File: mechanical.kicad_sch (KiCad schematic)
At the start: 0 parts

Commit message: SCH[Cleaning]:Updated Connectors not sure still, added sprate bat and ground connections, updated commincation conncetors. PCB[Layout]:Inital layout of compents need to fit on board size once tap connecton method is decided.
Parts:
- added FID1, FID2, FID3: Fiducial, Fiducial:Fiducial_0.5mm_Mask1mm, symbol Mechanical:Fiducial
- added H1, H2, H3, H4: MountingHole, MountingHole:MountingHole_3.2mm_M3, symbol Mechanical:MountingHole
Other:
- note added: "Fiducials"
- note added: "Mounting Holes"

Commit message: PCB[DRC, Grouding]: Need to seprate top ground planes, and possibliy bring caps to top side, started adressing drc errors. To fix: Via sizing on bms chip, ground planes and senstive grounds, trace matching sens and bal, connector finilzation, temp routing, logos and other silk screen, test points, review!
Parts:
- added H5: MountingHole, MountingHole:MountingHole_3.2mm_M3, symbol Mechanical:MountingHole
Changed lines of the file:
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@@
 	(rectangle
 		(start 101.6 83.82)
-		(end 139.7 101.6)
+		(end 139.7 109.22)
 		(stroke
 			(width 0.254)
@@
 					(unit 1)
 				)
+			)
+		)
+	)
+	(symbol
+		(lib_id "Mechanical:MountingHole")
+		(at 106.68 104.14 0)
+		(unit 1)
+		(body_style 1)
+		(exclude_from_sim no)
+		(in_bom no)
+		(on_board yes)
+		(in_pos_files yes)
+		(dnp no)
+		(fields_autoplaced yes)
+		(property "Reference" "H5"
+			(at 109.22 102.87 0)
+			(show_name no)
+			(do_not_autoplace no)
+			(effects
+				(font
+					(size 1.27 1.27)
+				)
+				(justify left)
+			)
+		)
+		(property "Value" "MountingHole"
+			(at 109.22 105.41 0)
+			(show_name no)
+			(do_not_autoplace no)
+			(effects
+				(font
+					(size 1.27 1.27)
+				)
+				(justify left)
+			)
+		)
+		(property "Footprint" "MountingHole:MountingHole_3.2mm_M3"
+			(at 106.68 104.14 0)
+			(hide yes)
+			(show_name no)
+			(do_not_autoplace no)
+			(effects
+				(font
+					(size 1.27 1.27)
+				)
+			)
+		)
+		(property "Datasheet" ""
+			(at 106.68 104.14 0)
+			(hide yes)
+			(show_name no)
+			(do_not_autoplace no)
+			(effects
+				(font
+					(size 1.27 1.27)
+				)
+			)
+		)
+		(property "Description" "Mounting Hole without connection"
+			(at 106.68 104.14 0)
+			(hide yes)
+			(show_name no)
+			(do_not_autoplace no)
+			(effects
+				(font
+					(size 1.27 1.27)
+				)
+			)
+		)
+		(instances
+			(project "bms_slave"
+				(path "/f9e05184-c88b-4a88-ae9c-ab2bdb32be7c/c5103ceb-5325-4a84-a025-9638a412984e/f4a7f626-808e-4d0f-b4d4-b24a2b39d327"
+					(reference "H5")
+					(unit 1)
+				)

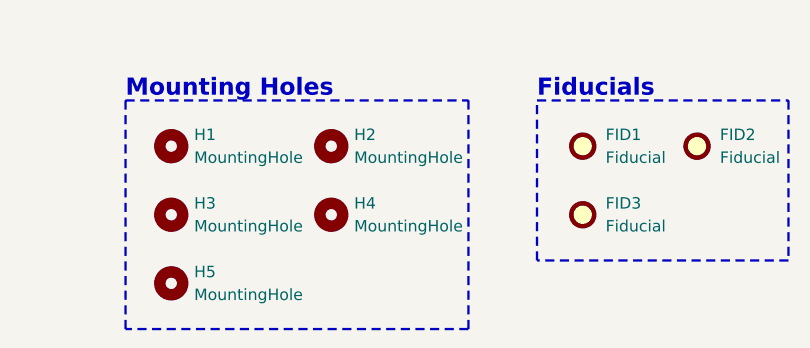
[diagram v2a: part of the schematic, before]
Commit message: PCB[Holes]: Updated hole positioning.
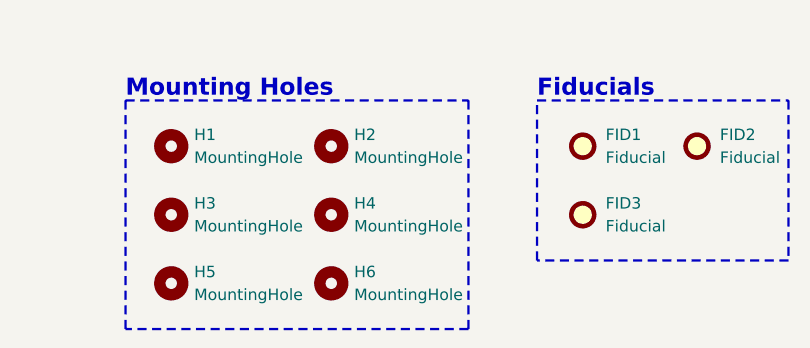
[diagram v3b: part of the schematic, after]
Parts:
- added H6: MountingHole, MountingHole:MountingHole_3.2mm_M3, symbol Mechanical:MountingHole
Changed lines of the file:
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@@
+	)
+	(symbol
+		(lib_id "Mechanical:MountingHole")
+		(at 124.46 104.14 0)
+		(unit 1)
+		(body_style 1)
+		(exclude_from_sim no)
+		(in_bom no)
+		(on_board yes)
+		(in_pos_files yes)
+		(dnp no)
+		(fields_autoplaced yes)
+		(property "Reference" "H6"
+			(at 127 102.87 0)
+			(show_name no)
+			(do_not_autoplace no)
+			(effects
+				(font
+					(size 1.27 1.27)
+				)
+				(justify left)
+			)
+		)
+		(property "Value" "MountingHole"
+			(at 127 105.41 0)
+			(show_name no)
+			(do_not_autoplace no)
+			(effects
+				(font
+					(size 1.27 1.27)
+				)
+				(justify left)
+			)
+		)
+		(property "Footprint" "MountingHole:MountingHole_3.2mm_M3"
+			(at 124.46 104.14 0)
+			(hide yes)
+			(show_name no)
+			(do_not_autoplace no)
+			(effects
+				(font
+					(size 1.27 1.27)
+				)
+			)
+		)
+		(property "Datasheet" ""
+			(at 124.46 104.14 0)
+			(hide yes)
+			(show_name no)
+			(do_not_autoplace no)
+			(effects
+				(font
+					(size 1.27 1.27)
+				)
+			)
+		)
+		(property "Description" "Mounting Hole without connection"
+			(at 124.46 104.14 0)
+			(hide yes)
+			(show_name no)
+			(do_not_autoplace no)
+			(effects
+				(font
+					(size 1.27 1.27)
+				)
+			)
+		)
+		(instances
+			(project "bms_slave"
+				(path "/f9e05184-c88b-4a88-ae9c-ab2bdb32be7c/c5103ceb-5325-4a84-a025-9638a412984e/f4a7f626-808e-4d0f-b4d4-b24a2b39d327"
+					(reference "H6")
+					(unit 1)
+				)
+			)
+		)
 	)
 	(symbol

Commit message: PCB[Silkscreen, DRC]: Though all drc erros minus one, not an issue just need to clear. Added silk logos
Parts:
- added G1: SAE Electric logo, remote_sae_electric_logo:SAE_Electric_Logo_10mm, symbol remote_sae_electric_logo:LOGO
- added G2: BMD Logo, remote_bmd_logo:BDM_Logo_50mm, symbol remote_bmd_logo:BMD LOGO
- added G3: Sparky Logo, remote_sparky_logo:Sparky_Logo_50mm, symbol remote_sparky_logo:LOGO

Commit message: PCB[Grounding, Heat]: Added some more pours for heat considerations for bjt, stiched more vias for heat consideration on balanace resistors. SCH[Notes, Block Diagram]: Working on spelling and notes updates, started block diagram.
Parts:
- removed G3: Sparky Logo, remote_sparky_logo:Sparky_Logo_50mm, symbol remote_sparky_logo:LOGO
- renumbered FID3 to FID2, FID2 to FID3, H3 to H2, H5 to H3, H2 to H4, H4 to H5
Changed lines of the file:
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@@
 		(dnp no)
 		(fields_autoplaced yes)
-		(property "Reference" "FID2"
+		(property "Reference" "FID3"
 			(at 167.64 87.63 0)
 			(show_name no)
@@
 			(project "bms_slave"
 				(path "/f9e05184-c88b-4a88-ae9c-ab2bdb32be7c/c5103ceb-5325-4a84-a025-9638a412984e/f4a7f626-808e-4d0f-b4d4-b24a2b39d327"
-					(reference "FID2")
+					(reference "FID3")
 					(unit 1)
 				)
@@
 		(dnp no)
 		(fields_autoplaced yes)
-		(property "Reference" "H5"
+		(property "Reference" "H3"
 			(at 109.22 102.87 0)
 			(show_name no)
@@
 			(project "bms_slave"
 				(path "/f9e05184-c88b-4a88-ae9c-ab2bdb32be7c/c5103ceb-5325-4a84-a025-9638a412984e/f4a7f626-808e-4d0f-b4d4-b24a2b39d327"
-					(reference "H5")
+					(reference "H3")
 					(unit 1)
 				)
@@
 		(dnp no)
 		(fields_autoplaced yes)
-		(property "Reference" "H3"
+		(property "Reference" "H2"
 			(at 109.22 95.25 0)
 			(show_name no)
@@
 			(project "bms_slave"
 				(path "/f9e05184-c88b-4a88-ae9c-ab2bdb32be7c/c5103ceb-5325-4a84-a025-9638a412984e/f4a7f626-808e-4d0f-b4d4-b24a2b39d327"
-					(reference "H3")
+					(reference "H2")
 					(unit 1)
 				)
@@
 		(dnp no)
 		(fields_autoplaced yes)
-		(property "Reference" "H4"
+		(property "Reference" "H5"
 			(at 127 95.25 0)
 			(show_name no)
@@
 			(project "bms_slave"
 				(path "/f9e05184-c88b-4a88-ae9c-ab2bdb32be7c/c5103ceb-5325-4a84-a025-9638a412984e/f4a7f626-808e-4d0f-b4d4-b24a2b39d327"
-					(reference "H4")
+					(reference "H5")
 					(unit 1)
 				)
@@
 		(dnp no)
 		(fields_autoplaced yes)
-		(property "Reference" "H2"
+		(property "Reference" "H4"
 			(at 127 87.63 0)
 			(show_name no)
@@
 			(project "bms_slave"
 				(path "/f9e05184-c88b-4a88-ae9c-ab2bdb32be7c/c5103ceb-5325-4a84-a025-9638a412984e/f4a7f626-808e-4d0f-b4d4-b24a2b39d327"
-					(reference "H2")
+					(reference "H4")
 					(unit 1)
 				)
@@
 		(dnp no)
 		(fields_autoplaced yes)
-		(property "Reference" "FID3"
+		(property "Reference" "FID2"
 			(at 154.94 95.25 0)
 			(show_name no)
@@
 			(project "bms_slave"
 				(path "/f9e05184-c88b-4a88-ae9c-ab2bdb32be7c/c5103ceb-5325-4a84-a025-9638a412984e/f4a7f626-808e-4d0f-b4d4-b24a2b39d327"
-					(reference "FID3")
+					(reference "FID2")
 					(unit 1)
 				)
-			)
-		)
-	)
-	(symbol
-		(lib_id "remote_sparky_logo:LOGO")
-		(at 214.63 129.54 0)
-		(unit 1)
-		(body_style 0)
-		(exclude_from_sim no)
-		(in_bom yes)
-		(on_board yes)
-		(in_pos_files yes)
-		(dnp no)
-		(property "Reference" "G3"
-			(at 214.63 105.1737 0)
-			(hide yes)
-			(show_name no)
-			(do_not_autoplace no)
-			(effects
-				(font
-					(size 1.27 1.27)
-				)
-			)
-		)
-		(property "Value" "Sparky Logo"
-			(at 209.55 106.68 0)
-			(show_name no)
-			(do_not_autoplace no)
-			(effects
-				(font
-					(size 1.27 1.27)
-				)
-				(justify left)
-			)
-		)
-		(property "Footprint" "remote_sparky_logo:Sparky_Logo_50mm"
-			(at 214.63 129.54 0)
-			(hide yes)
-			(show_name no)
-			(do_not_autoplace no)
-			(effects
-				(font
-					(size 1.27 1.27)
-				)
-			)
-		)
-		(property "Datasheet" "N/A"
-			(at 214.63 129.54 0)
-			(hide yes)
-			(show_name no)
-			(do_not_autoplace no)
-			(effects
-				(font
-					(size 1.27 1.27)
-				)
-			)
-		)
-		(property "Description" "Sparky Logo."
-			(at 214.63 129.54 0)
-			(hide yes)
-			(show_name no)
-			(do_not_autoplace no)
-			(effects
-				(font
-					(size 1.27 1.27)
-				)
-			)
-		)
-		(property "Manufacturer" "BDM"
-			(at 214.63 129.54 0)
-			(hide yes)
-			(show_name no)
-			(do_not_autoplace no)
-			(effects
-				(font
-					(size 1.27 1.27)
-				)
-			)
-		)
-		(property "Manufacturer Part Number" "Sparky Logo"
-			(at 214.63 129.54 0)
-			(hide yes)
-			(show_name no)
-			(do_not_autoplace no)
-			(effects
-				(font
-					(size 1.27 1.27)
-				)
-			)
-		)
-		(property "Vendor" ""
-			(at 214.63 129.54 0)
-			(hide yes)
-			(show_name no)
-			(do_not_autoplace no)
-			(effects
-				(font
-					(size 1.27 1.27)
-				)
-			)
-		)
-		(property "Vendor Part Number" ""
-			(at 214.63 129.54 0)
-			(hide yes)
-			(show_name no)
-			(do_not_autoplace no)
-			(effects
-				(font
-					(size 1.27 1.27)
-				)
-			)
-		)
-		(property "Mass (g)" ""
-			(at 214.63 129.54 0)
-			(hide yes)
-			(show_name no)
-			(do_not_autoplace no)
-			(effects
-				(font
-					(size 1.27 1.27)
-				)
-			)
-		)
-		(property "RQjC (C/W)" ""
-			(at 214.63 129.54 0)
-			(hide yes)
-			(show_name no)
-			(do_not_autoplace no)
-			(effects
-				(font
-					(size 1.27 1.27)
-				)
-			)
-		)
-		(property "RQjC_top (C/W)" ""
-			(at 214.63 129.54 0)
-			(hide yes)
-			(show_name no)
-			(do_not_autoplace no)
-			(effects
-				(font
-					(size 1.27 1.27)
-				)
-			)
-		)
-		(property "Temp_max (C)" ""
-			(at 214.63 129.54 0)
-			(hide yes)
-			(show_name no)
-			(do_not_autoplace no)
-			(effects
-				(font
-					(size 1.27 1.27)
-				)
-			)
-		)
-		(property "Temp_min (C)" ""
-			(at 214.63 129.54 0)
-			(hide yes)
-			(show_name no)
-			(do_not_autoplace no)
-			(effects
-				(font
-					(size 1.27 1.27)
-				)
-			)
-		)
-		(property "Power Dissipation (W)" ""
-			(at 214.63 129.54 0)
-			(hide yes)
-			(show_name no)
-			(do_not_autoplace no)
-			(effects
-				(font
-					(size 1.27 1.27)
-				)
-			)
-		)
-		(property "Rate" ""
-			(at 214.63 129.54 0)
-			(hide yes)
-			(show_name no)
-			(do_not_autoplace no)
-			(effects
-				(font
-					(size 1.27 1.27)
-				)
-			)
-		)
-		(property "SAP Code" ""
-			(at 214.63 129.54 0)
-			(hide yes)
-			(show_name no)
-			(do_not_autoplace no)
-			(effects
-				(font
-					(size 1.27 1.27)
-				)
-			)
-		)
-		(instances
-			(project "bms_slave"
-				(path "/f9e05184-c88b-4a88-ae9c-ab2bdb32be7c/c5103ceb-5325-4a84-a025-9638a412984e/f4a7f626-808e-4d0f-b4d4-b24a2b39d327"
-					(reference "G3")
-					(unit 1)
-				)

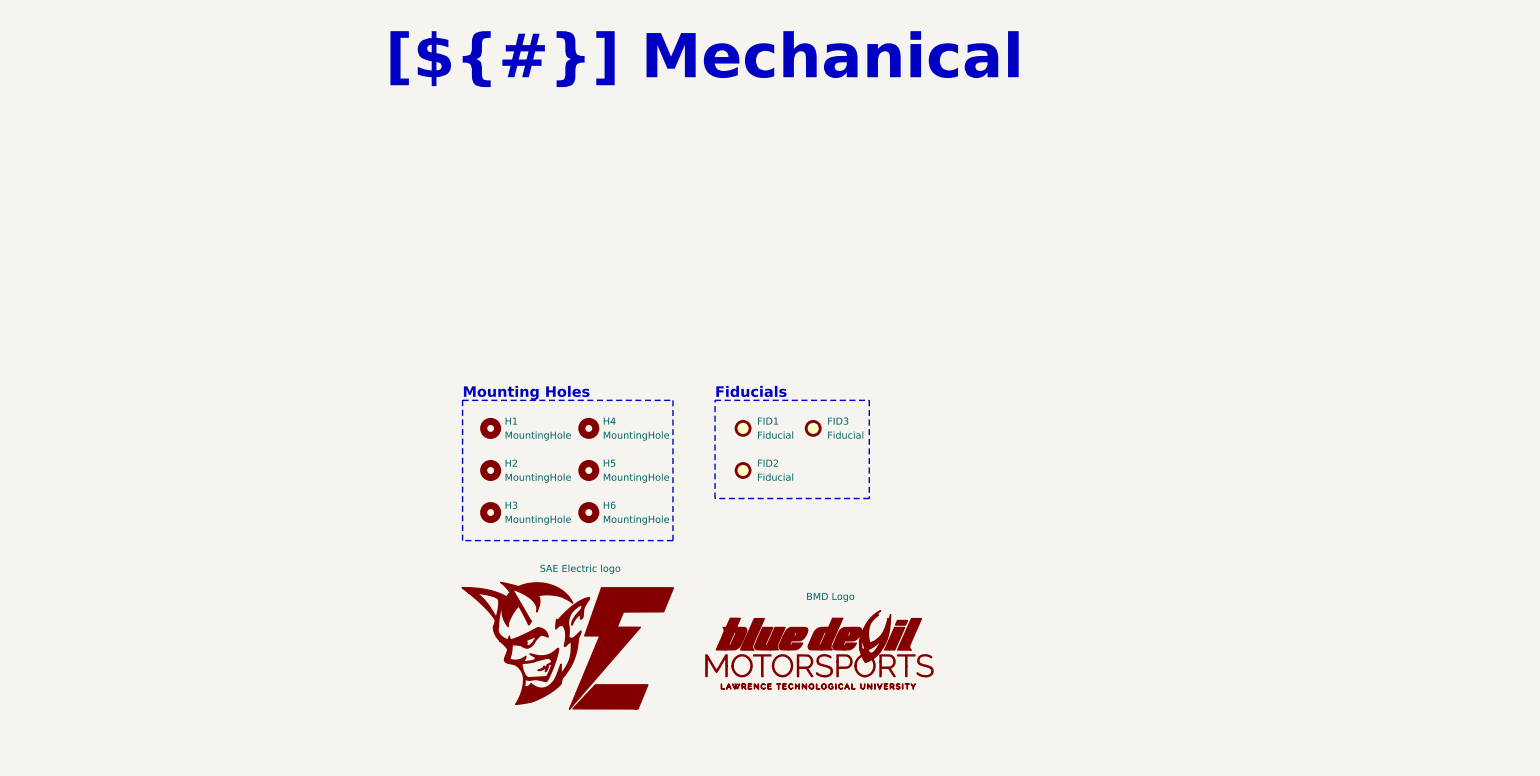
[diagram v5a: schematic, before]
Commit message: PCB[Test Points, Mechanical, Silk]: Finalized Mounting Points, Added Testpoints with adjecent silkscreen labels. SCH[Test Points, Notes]: Added/Updated notes for all pages, cleaned up errors spelling ect.
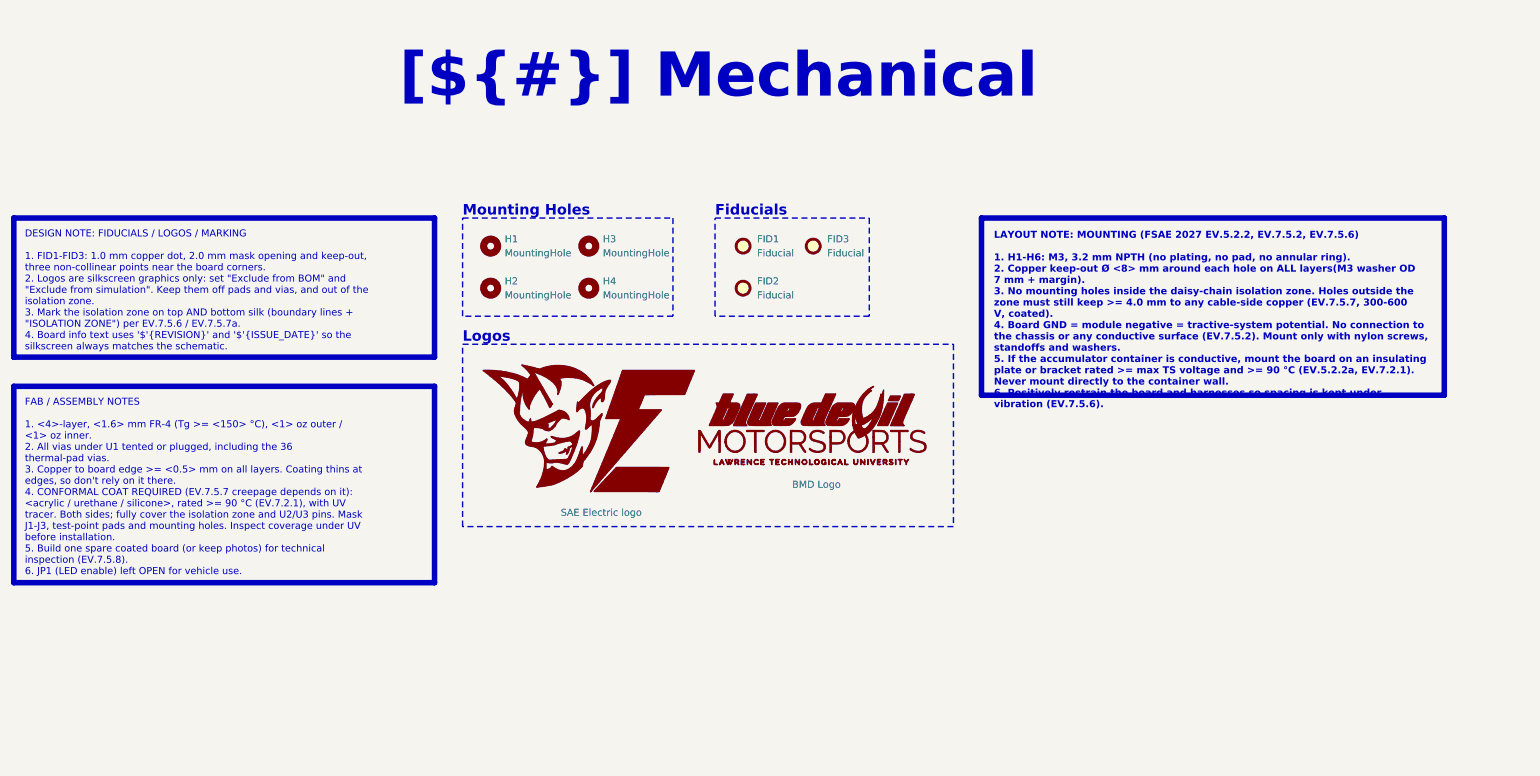
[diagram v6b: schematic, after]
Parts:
- removed H5, H6: MountingHole, MountingHole:MountingHole_3.2mm_M3, symbol Mechanical:MountingHole
- G1, G2: now left out of the parts list
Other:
- note added: "Logos"
- moved on the sheet: FID1, FID2, FID3, H1, H2, H3, H4

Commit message: PCB&SCH[Fid]: Added 3 fiductals on the back for fab.
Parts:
- added FID4, FID5, FID6: Fiducial, Fiducial:Fiducial_0.5mm_Mask1mm, symbol Mechanical:Fiducial
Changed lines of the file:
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@@
 	(rectangle
 		(start 147.32 50.8)
-		(end 175.26 68.58)
+		(end 190.5 68.58)
 		(stroke
 			(width 0.254)
@@
 	(symbol
 		(lib_id "Mechanical:Fiducial")
+		(at 165.1 63.5 0)
+		(unit 1)
+		(body_style 1)
+		(exclude_from_sim no)
+		(in_bom no)
+		(on_board yes)
+		(in_pos_files yes)
+		(dnp no)
+		(fields_autoplaced yes)
+		(property "Reference" "FID4"
+			(at 167.64 62.23 0)
+			(show_name no)
+			(do_not_autoplace no)
+			(effects
+				(font
+					(size 1.27 1.27)
+				)
+				(justify left)
+			)
+		)
+		(property "Value" "Fiducial"
+			(at 167.64 64.77 0)
+			(show_name no)
+			(do_not_autoplace no)
+			(effects
+				(font
+					(size 1.27 1.27)
+				)
+				(justify left)
+			)
+		)
+		(property "Footprint" "Fiducial:Fiducial_0.5mm_Mask1mm"
+			(at 165.1 63.5 0)
+			(hide yes)
+			(show_name no)
+			(do_not_autoplace no)
+			(effects
+				(font
+					(size 1.27 1.27)
+				)
+			)
+		)
+		(property "Datasheet" ""
+			(at 165.1 63.5 0)
+			(hide yes)
+			(show_name no)
+			(do_not_autoplace no)
+			(effects
+				(font
+					(size 1.27 1.27)
+				)
+			)
+		)
+		(property "Description" "Fiducial Marker"
+			(at 165.1 63.5 0)
+			(hide yes)
+			(show_name no)
+			(do_not_autoplace no)
+			(effects
+				(font
+					(size 1.27 1.27)
+				)
+			)
+		)
+		(instances
+			(project "bms_slave"
+				(path "/f9e05184-c88b-4a88-ae9c-ab2bdb32be7c/c5103ceb-5325-4a84-a025-9638a412984e/f4a7f626-808e-4d0f-b4d4-b24a2b39d327"
+					(reference "FID4")
+					(unit 1)
+				)
+			)
+		)
+	)
+	(symbol
+		(lib_id "Mechanical:Fiducial")
 		(at 165.1 55.88 0)
 		(unit 1)
@@
 	(symbol
 		(lib_id "Mechanical:Fiducial")
+		(at 177.8 63.5 0)
+		(unit 1)
+		(body_style 1)
+		(exclude_from_sim no)
+		(in_bom no)
+		(on_board yes)
+		(in_pos_files yes)
+		(dnp no)
+		(fields_autoplaced yes)
+		(property "Reference" "FID6"
+			(at 180.34 62.23 0)
+			(show_name no)
+			(do_not_autoplace no)
+			(effects
+				(font
+					(size 1.27 1.27)
+				)
+				(justify left)
+			)
+		)
+		(property "Value" "Fiducial"
+			(at 180.34 64.77 0)
+			(show_name no)
+			(do_not_autoplace no)
+			(effects
+				(font
+					(size 1.27 1.27)
+				)
+				(justify left)
+			)
+		)
+		(property "Footprint" "Fiducial:Fiducial_0.5mm_Mask1mm"
+			(at 177.8 63.5 0)
+			(hide yes)
+			(show_name no)
+			(do_not_autoplace no)
+			(effects
+				(font
+					(size 1.27 1.27)
+				)
+			)
+		)
+		(property "Datasheet" ""
+			(at 177.8 63.5 0)
+			(hide yes)
+			(show_name no)
+			(do_not_autoplace no)
+			(effects
+				(font
+					(size 1.27 1.27)
+				)
+			)
+		)
+		(property "Description" "Fiducial Marker"
+			(at 177.8 63.5 0)
+			(hide yes)
+			(show_name no)
+			(do_not_autoplace no)
+			(effects
+				(font
+					(size 1.27 1.27)
+				)
+			)
+		)
+		(instances
+			(project "bms_slave"
+				(path "/f9e05184-c88b-4a88-ae9c-ab2bdb32be7c/c5103ceb-5325-4a84-a025-9638a412984e/f4a7f626-808e-4d0f-b4d4-b24a2b39d327"
+					(reference "FID6")
+					(unit 1)
+				)
+			)
+		)
+	)
+	(symbol
+		(lib_id "Mechanical:Fiducial")
 		(at 152.4 55.88 0)
 		(unit 1)
@@
 					(unit 1)
 				)
+			)
+		)
+	)
+	(symbol
+		(lib_id "Mechanical:Fiducial")
+		(at 177.8 55.88 0)
+		(unit 1)
+		(body_style 1)
+		(exclude_from_sim no)
+		(in_bom no)
+		(on_board yes)
+		(in_pos_files yes)
+		(dnp no)
+		(fields_autoplaced yes)
+		(property "Reference" "FID5"
+			(at 180.34 54.61 0)
+			(show_name no)
+			(do_not_autoplace no)
+			(effects
+				(font
+					(size 1.27 1.27)
+				)
+				(justify left)
+			)
+		)
+		(property "Value" "Fiducial"
+			(at 180.34 57.15 0)
+			(show_name no)
+			(do_not_autoplace no)
+			(effects
+				(font
+					(size 1.27 1.27)
+				)
+				(justify left)
+			)
+		)
+		(property "Footprint" "Fiducial:Fiducial_0.5mm_Mask1mm"
+			(at 177.8 55.88 0)
+			(hide yes)
+			(show_name no)
+			(do_not_autoplace no)
+			(effects
+				(font
+					(size 1.27 1.27)
+				)
+			)
+		)
+		(property "Datasheet" ""
+			(at 177.8 55.88 0)
+			(hide yes)
+			(show_name no)
+			(do_not_autoplace no)
+			(effects
+				(font
+					(size 1.27 1.27)
+				)
+			)
+		)
+		(property "Description" "Fiducial Marker"
+			(at 177.8 55.88 0)
+			(hide yes)
+			(show_name no)
+			(do_not_autoplace no)
+			(effects
+				(font
+					(size 1.27 1.27)
+				)
+			)
+		)
+		(instances
+			(project "bms_slave"
+				(path "/f9e05184-c88b-4a88-ae9c-ab2bdb32be7c/c5103ceb-5325-4a84-a025-9638a412984e/f4a7f626-808e-4d0f-b4d4-b24a2b39d327"
+					(reference "FID5")
+					(unit 1)
+				)
